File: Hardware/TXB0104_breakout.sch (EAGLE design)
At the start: 9 parts

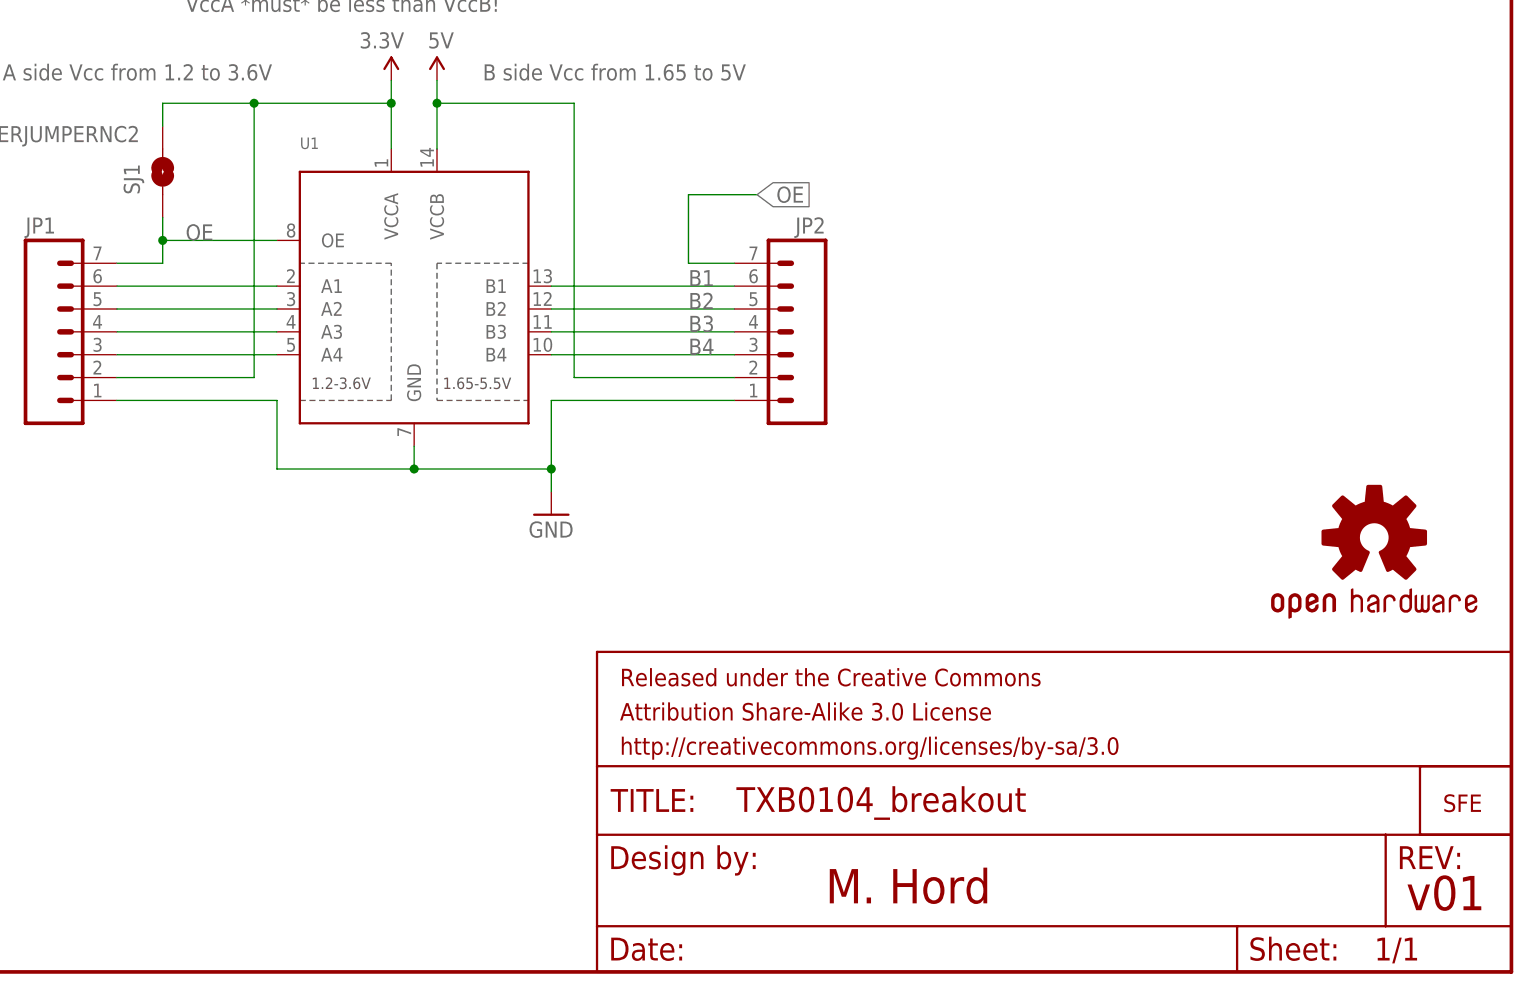
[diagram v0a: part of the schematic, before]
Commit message: Changes for production  - Made vias .020"  - Fixed a couple of clearance errors  - Add silk for jumper on top  - Move C packages to true 0603  - Change version number
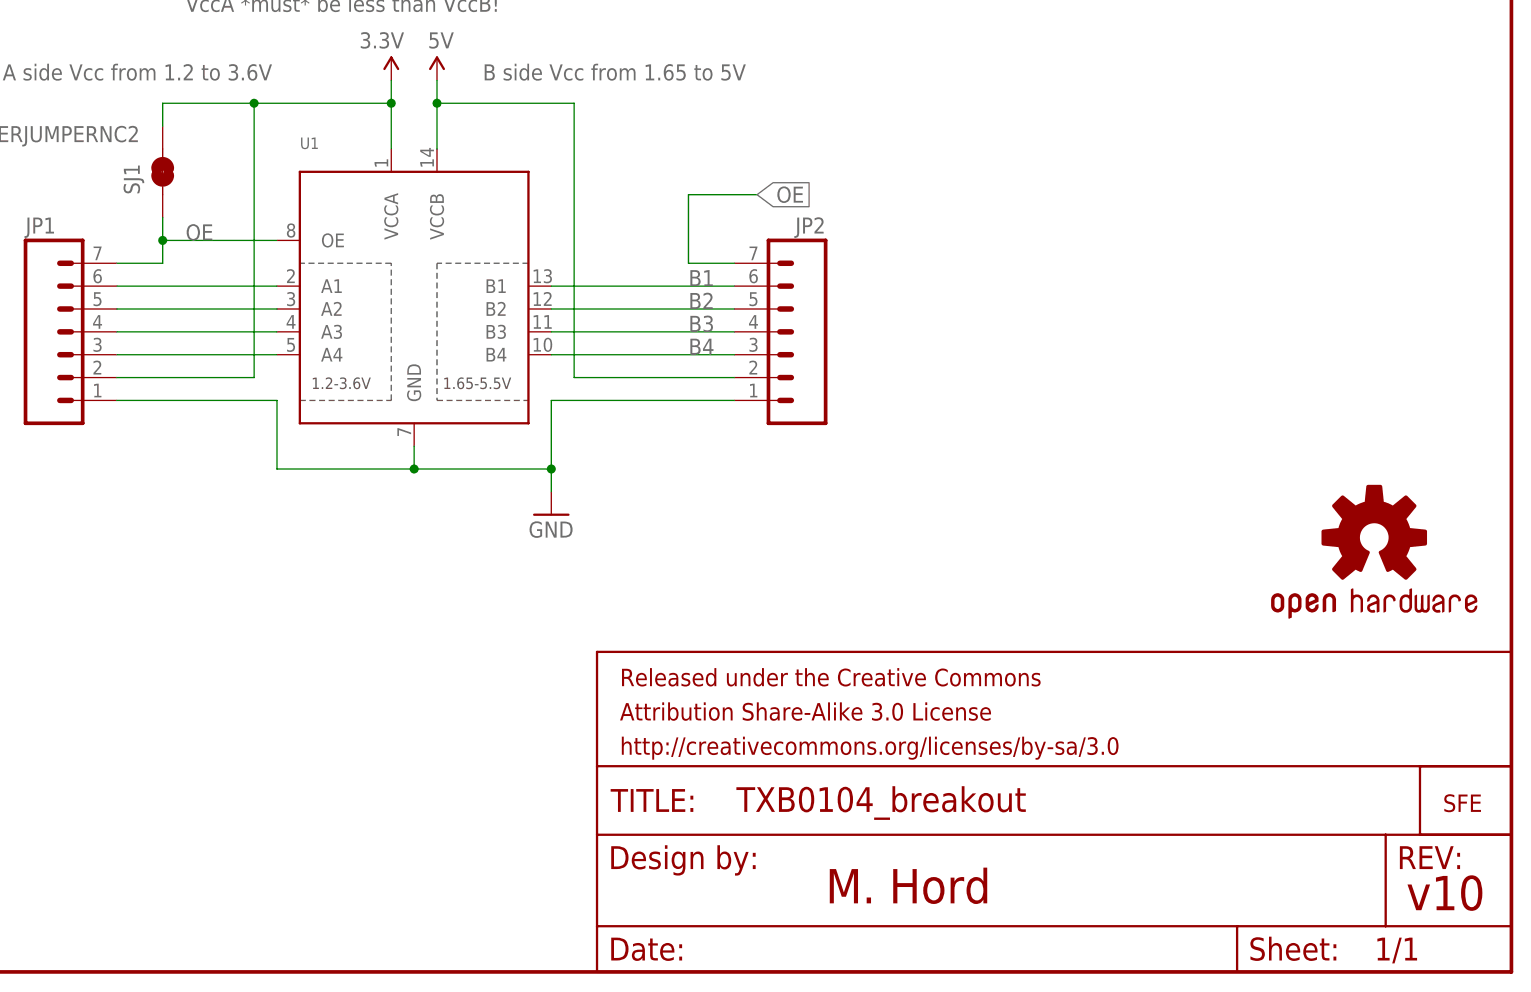
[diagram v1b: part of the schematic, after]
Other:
- note added: "v10"
- note removed: "v01"
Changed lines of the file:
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@@
 <text x="134.62" y="99.06" size="1.778" layer="95">B side Vcc from 1.65 to 5V</text>
 <text x="101.6" y="106.68" size="1.778" layer="95">VccA *must* be less than VccB!</text>
-<text x="237.236" y="6.858" size="3.81" layer="94">v01</text>
+<text x="237.236" y="6.858" size="3.81" layer="94">v10</text>
 <text x="172.72" y="7.62" size="3.81" layer="94">M. Hord</text>
+<wire x1="99.06" y1="88.138" x2="99.06" y2="89.916" width="0.1524" layer="94"/>
 </plain>
 <instances>

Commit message: Production readied
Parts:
- added FID1, FID2: FIDUCIALUFIDUCIAL, SparkFun-Aesthetics:FIDUCIALUFIDUCIAL
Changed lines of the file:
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@@
 <part name="GND2" library="SparkFun-Aesthetics" deviceset="GND" device=""/>
 <part name="GND3" library="SparkFun-Aesthetics" deviceset="GND" device=""/>
+<part name="FID1" library="SparkFun-Aesthetics" deviceset="FIDUCIAL" device="UFIDUCIAL"/>
+<part name="FID2" library="SparkFun-Aesthetics" deviceset="FIDUCIAL" device="UFIDUCIAL"/>
 </parts>
 <sheets>
@@
 <instance part="GND2" gate="1" x="134.62" y="124.46"/>
 <instance part="GND3" gate="1" x="124.46" y="124.46"/>
+<instance part="FID1" gate="G$1" x="241.3" y="33.02"/>
+<instance part="FID2" gate="G$1" x="236.22" y="33.02"/>
 </instances>
 <busses>
